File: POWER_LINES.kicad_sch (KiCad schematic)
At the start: 50 parts, among them J11 1717020, J12 1717020, J6 1730405, J8 1717020, J9 1717020, K3 G2R-1A-E DC5, K4 G2R-1A-E DC5, K5 G2R-1A-E DC5, K6 G2R-1A-E DC5, Q3 AO3400A, Q4 AO3400A

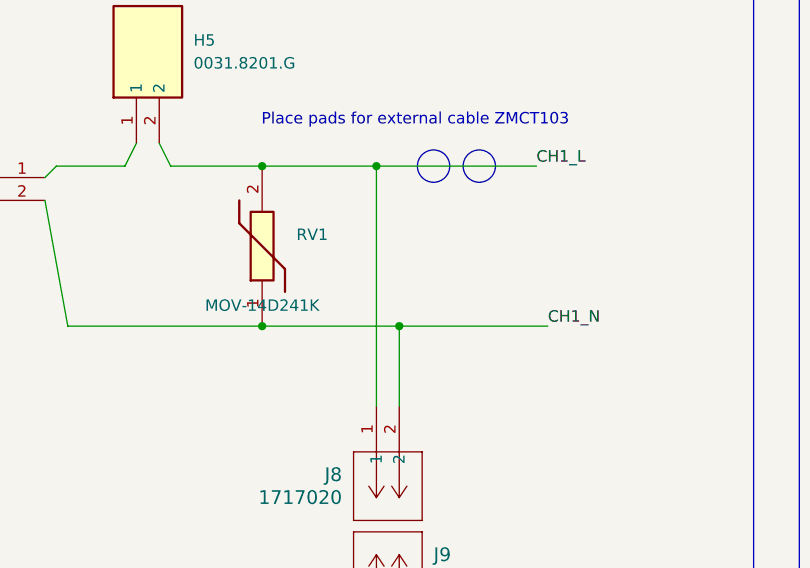
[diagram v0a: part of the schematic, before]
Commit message: add usb 2.0 speed selector
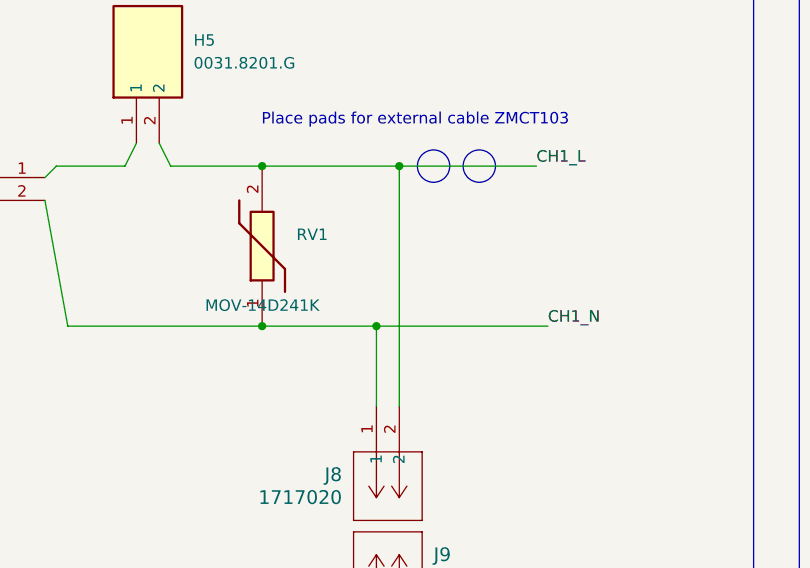
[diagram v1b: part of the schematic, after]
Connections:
- net CH1_L: now also J8.2; no longer J8.1
- net CH1_N: now also J8.1; no longer J8.2
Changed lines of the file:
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@@
 	)
 	(junction
-		(at 203.2 102.87)
+		(at 123.19 49.53)
 		(diameter 0)
 		(color 0 0 0 0)
 	)
 	(junction
-		(at 110.49 31.75)
+		(at 203.2 102.87)
 		(diameter 0)
 		(color 0 0 0 0)
 	)
 	(junction
-		(at 125.73 49.53)
+		(at 110.49 31.75)
 		(diameter 0)
 		(color 0 0 0 0)
@@
 	)
 	(junction
+		(at 125.73 31.75)
+		(diameter 0)
+		(color 0 0 0 0)
+	)
+	(junction
 		(at 66.04 137.16)
 		(diameter 0)
@@
 		(color 0 0 0 0)
 	)
-	(junction
-		(at 123.19 31.75)
-		(diameter 0)
-		(color 0 0 0 0)
-	)
 	(wire
 		(pts
@@
 	(wire
 		(pts
+			(xy 125.73 31.75) (xy 140.97 31.75)
+		)
+		(stroke
+			(width 0)
+			(type default)
+		)
+	)
+	(wire
+		(pts
 			(xy 25.4 158.75) (xy 33.02 158.75)
 		)
@@
 	(wire
 		(pts
-			(xy 110.49 31.75) (xy 140.97 31.75)
+			(xy 110.49 31.75) (xy 125.73 31.75)
 		)
 		(stroke
@@
 	(wire
 		(pts
-			(xy 125.73 49.53) (xy 125.73 58.42)
-		)
-		(stroke
-			(width 0)
-			(type default)
-		)
-	)
-	(wire
-		(pts
 			(xy 59.69 137.16) (xy 66.04 137.16)
 		)
@@
 	(wire
 		(pts
-			(xy 99.06 29.21) (xy 100.33 31.75)
+			(xy 123.19 49.53) (xy 123.19 58.42)
 		)
 		(stroke
@@
 	(wire
 		(pts
-			(xy 203.2 119.38) (xy 203.2 137.16)
+			(xy 99.06 29.21) (xy 100.33 31.75)
 		)
 		(stroke
@@
 	(wire
 		(pts
-			(xy 125.73 49.53) (xy 142.24 49.53)
+			(xy 203.2 119.38) (xy 203.2 137.16)
 		)
 		(stroke
@@
 	(wire
 		(pts
-			(xy 123.19 31.75) (xy 123.19 58.42)
+			(xy 204.47 45.72) (xy 204.47 62.23)
 		)
 		(stroke
@@
 	(wire
 		(pts
-			(xy 204.47 45.72) (xy 204.47 62.23)
+			(xy 204.47 29.21) (xy 204.47 38.1)
 		)
 		(stroke
@@
 	(wire
 		(pts
-			(xy 204.47 29.21) (xy 204.47 38.1)
+			(xy 218.44 53.34) (xy 218.44 59.69)
 		)
 		(stroke
@@
 	(wire
 		(pts
-			(xy 218.44 53.34) (xy 218.44 59.69)
+			(xy 266.7 135.89) (xy 271.78 135.89)
 		)
 		(stroke
@@
 	(wire
 		(pts
-			(xy 266.7 135.89) (xy 271.78 135.89)
+			(xy 113.03 168.91) (xy 116.84 168.91)
 		)
 		(stroke
@@
 	(wire
 		(pts
-			(xy 113.03 168.91) (xy 116.84 168.91)
+			(xy 66.04 173.99) (xy 66.04 176.53)
 		)
 		(stroke
@@
 	(wire
 		(pts
-			(xy 66.04 173.99) (xy 66.04 176.53)
+			(xy 132.08 125.73) (xy 132.08 123.19)
 		)
 		(stroke
@@
 	(wire
 		(pts
-			(xy 132.08 125.73) (xy 132.08 123.19)
+			(xy 125.73 31.75) (xy 125.73 58.42)
 		)
 		(stroke
@@
 	(wire
 		(pts
+			(xy 123.19 49.53) (xy 142.24 49.53)
+		)
+		(stroke
+			(width 0)
+			(type default)
+		)
+	)
+	(wire
+		(pts
 			(xy 95.25 31.75) (xy 96.52 29.21)
 		)
@@
 	(wire
 		(pts
-			(xy 110.49 49.53) (xy 125.73 49.53)
+			(xy 110.49 49.53) (xy 123.19 49.53)
 		)
 		(stroke
@@
 		(in_pos_files yes)
 		(dnp no)
-		(fields_autoplaced yes)
 		(property "Reference" "J9"
 			(at 129.54 74.9299 90)

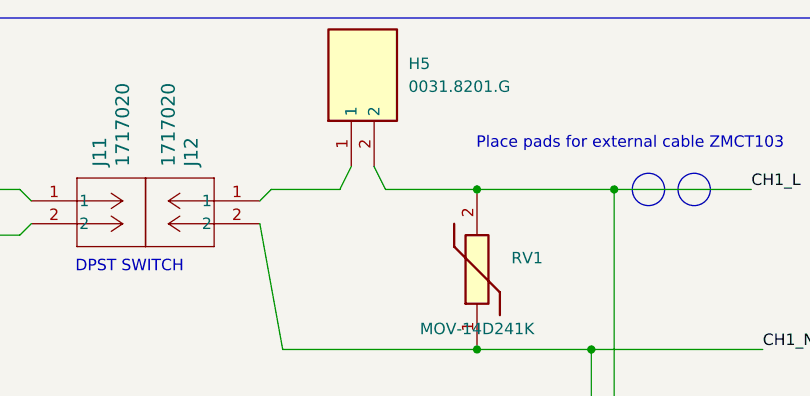
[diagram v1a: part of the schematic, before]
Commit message: add leds
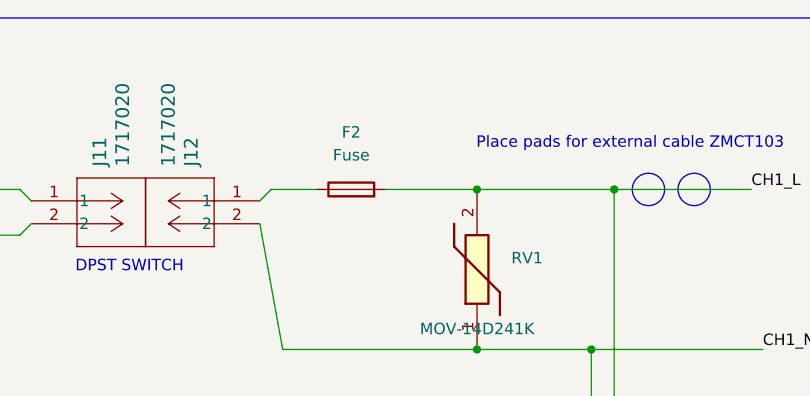
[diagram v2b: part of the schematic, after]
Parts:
- F2: renamed from H5; value 0031.8201.G -> Fuse; symbol SamacSys_Parts:0031.8201.G -> Device:Fuse
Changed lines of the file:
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@@
 	(wire
 		(pts
-			(xy 100.33 31.75) (xy 110.49 31.75)
-		)
-		(stroke
-			(width 0)
-			(type default)
-		)
-	)
-	(wire
-		(pts
 			(xy 60.96 107.95) (xy 60.96 104.14)
 		)
@@
 	(wire
 		(pts
-			(xy 87.63 31.75) (xy 95.25 31.75)
+			(xy 87.63 31.75) (xy 92.71 31.75)
 		)
 		(stroke
@@
 	(wire
 		(pts
-			(xy 99.06 29.21) (xy 100.33 31.75)
+			(xy 100.33 31.75) (xy 110.49 31.75)
 		)
 		(stroke
@@
 	(wire
 		(pts
-			(xy 95.25 31.75) (xy 96.52 29.21)
-		)
-		(stroke
-			(width 0)
-			(type default)
-		)
-	)
-	(wire
-		(pts
 			(xy 203.2 100.33) (xy 203.2 102.87)
 		)
@@
 	)
 	(symbol
-		(lib_id "SamacSys_Parts:0031.8201.G")
-		(at 96.52 29.21 90)
+		(lib_id "Device:Fuse")
+		(at 96.52 31.75 90)
 		(unit 1)
 		(body_style 1)
@@
 		(dnp no)
 		(fields_autoplaced yes)
-		(property "Reference" "H5"
-			(at 102.87 17.7799 90)
+		(property "Reference" "F2"
+			(at 96.52 25.4 90)
 			(show_name no)
 			(do_not_autoplace no)
@@
 					(size 1.27 1.27)
 				)
-				(justify right)
 			)
 		)
-		(property "Value" "0031.8201.G"
-			(at 102.87 20.3199 90)
+		(property "Value" "Fuse"
+			(at 96.52 27.94 90)
 			(show_name no)
 			(do_not_autoplace no)
@@
 					(size 1.27 1.27)
 				)
-				(justify right)
 			)
 		)
 		(property "Footprint" "SmartSupplyLib:fuse holder"
-			(at 191.44 12.7 0)
+			(at 96.52 33.528 90)
 			(hide yes)
 			(show_name no)
@@
 					(size 1.27 1.27)
 				)
-				(justify left top)
 			)
 		)
 		(property "Datasheet" "https://www.schurter.com/en/datasheet/ogn"
-			(at 291.44 12.7 0)
+			(at 96.52 31.75 0)
 			(hide yes)
 			(show_name no)
@@
 					(size 1.27 1.27)
 				)
-				(justify left top)
 			)
 		)
-		(property "Description" "OGN for THT 22.5mm"
-			(at 96.52 29.21 0)
+		(property "Description" "Fuse"
+			(at 96.52 31.75 0)
 			(hide yes)
 			(show_name no)
@@
 		)
 		(property "Height" "12.7"
-			(at 491.44 12.7 0)
+			(at 491.44 15.24 0)
 			(hide yes)
 			(show_name no)
@@
 		)
 		(property "Mouser Part Number" "693-0031.8201.G"
-			(at 591.44 12.7 0)
+			(at 591.44 15.24 0)
 			(hide yes)
 			(show_name no)
@@
 		)
 		(property "Mouser Price/Stock" "https://www.mouser.co.uk/ProductDetail/Schurter/0031.8201.G?qs=53fxdJjyGHQ26HnfkWkpvg%3D%3D"
-			(at 691.44 12.7 0)
+			(at 691.44 15.24 0)
 			(hide yes)
 			(show_name no)
@@
 		)
 		(property "Manufacturer_Name" "SCHURTER"
-			(at 791.44 12.7 0)
+			(at 791.44 15.24 0)
 			(hide yes)
 			(show_name no)
@@
 		)
 		(property "Manufacturer_Part_Number" "0031.8201.G"
-			(at 891.44 12.7 0)
+			(at 891.44 15.24 0)
 			(hide yes)
 			(show_name no)
@@
 			(project "smart_supply"
 				(path "/487ef637-7a03-4925-80c1-798e0c6f0bbd/34ab41b0-567d-4411-99e8-070d64ace837"
-					(reference "H5")
+					(reference "F2")
 					(unit 1)
 				)

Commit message: minimal change
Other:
- moved on the sheet: F2, RV1
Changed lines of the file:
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@@
 	)
 	(circle
-		(center 134.62 31.75)
+		(center 134.62 22.86)
 		(radius 1.7961)
 		(stroke
@@
 	)
 	(circle
-		(center 129.54 31.75)
+		(center 129.54 22.86)
 		(radius 1.7961)
 		(stroke
@@
 	(text "Place pads for external cable ZMCT103"
 		(exclude_from_sim no)
-		(at 127.508 26.67 0)
+		(at 127.508 17.78 0)
 		(effects
 			(font
@@
 	)
 	(junction
-		(at 110.49 31.75)
+		(at 110.49 22.86)
 		(diameter 0)
 		(color 0 0 0 0)
@@
 	)
 	(junction
-		(at 125.73 31.75)
+		(at 125.73 22.86)
 		(diameter 0)
 		(color 0 0 0 0)
@@
 	(wire
 		(pts
+			(xy 86.36 35.56) (xy 87.63 35.56)
+		)
+		(stroke
+			(width 0)
+			(type default)
+		)
+	)
+	(wire
+		(pts
 			(xy 193.04 83.82) (xy 193.04 85.09)
 		)
@@
 	(wire
 		(pts
+			(xy 110.49 22.86) (xy 110.49 26.67)
+		)
+		(stroke
+			(width 0)
+			(type default)
+		)
+	)
+	(wire
+		(pts
 			(xy 127 101.6) (xy 132.08 101.6)
 		)
@@
 	(wire
 		(pts
-			(xy 125.73 31.75) (xy 140.97 31.75)
+			(xy 125.73 22.86) (xy 140.97 22.86)
 		)
 		(stroke
@@
 	(wire
 		(pts
+			(xy 87.63 49.53) (xy 110.49 49.53)
+		)
+		(stroke
+			(width 0)
+			(type default)
+		)
+	)
+	(wire
+		(pts
 			(xy 132.08 152.4) (xy 135.89 152.4)
 		)
@@
 	(wire
 		(pts
-			(xy 110.49 31.75) (xy 125.73 31.75)
+			(xy 110.49 22.86) (xy 125.73 22.86)
 		)
 		(stroke
@@
 	(wire
 		(pts
-			(xy 88.9 49.53) (xy 110.49 49.53)
-		)
-		(stroke
-			(width 0)
-			(type default)
-		)
-	)
-	(wire
-		(pts
 			(xy 217.17 127) (xy 217.17 133.35)
 		)
@@
 	(wire
 		(pts
-			(xy 88.9 49.53) (xy 86.36 35.56)
-		)
-		(stroke
-			(width 0)
-			(type default)
-		)
-	)
-	(wire
-		(pts
-			(xy 87.63 31.75) (xy 92.71 31.75)
+			(xy 102.87 186.69) (xy 113.03 186.69)
 		)
 		(stroke
@@
 	(wire
 		(pts
-			(xy 102.87 186.69) (xy 113.03 186.69)
+			(xy 87.63 35.56) (xy 87.63 49.53)
 		)
 		(stroke
@@
 	(wire
 		(pts
+			(xy 87.63 22.86) (xy 92.71 22.86)
+		)
+		(stroke
+			(width 0)
+			(type default)
+		)
+	)
+	(wire
+		(pts
+			(xy 110.49 44.45) (xy 110.49 49.53)
+		)
+		(stroke
+			(width 0)
+			(type default)
+		)
+	)
+	(wire
+		(pts
 			(xy 125.73 85.09) (xy 149.86 85.09)
 		)
@@
 	(wire
 		(pts
-			(xy 100.33 31.75) (xy 110.49 31.75)
+			(xy 100.33 22.86) (xy 110.49 22.86)
 		)
 		(stroke
@@
 	(wire
 		(pts
+			(xy 87.63 33.02) (xy 86.36 33.02)
+		)
+		(stroke
+			(width 0)
+			(type default)
+		)
+	)
+	(wire
+		(pts
 			(xy 247.65 55.88) (xy 247.65 62.23)
 		)
@@
 	(wire
 		(pts
-			(xy 86.36 33.02) (xy 87.63 31.75)
+			(xy 87.63 33.02) (xy 87.63 22.86)
 		)
 		(stroke
@@
 	(wire
 		(pts
-			(xy 125.73 31.75) (xy 125.73 58.42)
+			(xy 125.73 22.86) (xy 125.73 58.42)
 		)
 		(stroke
@@
 	)
 	(label "CH1_L"
-		(at 140.97 31.75 0)
+		(at 140.97 22.86 0)
 		(effects
 			(font
@@
 	(symbol
 		(lib_id "SmartSupplyLib:MOV-14D241K")
-		(at 110.49 49.53 90)
+		(at 110.49 44.45 90)
 		(unit 1)
 		(body_style 1)
@@
 		(dnp no)
 		(property "Reference" "RV1"
-			(at 114.3 39.3699 90)
+			(at 114.3 34.2899 90)
 			(show_name no)
 			(do_not_autoplace no)
@@
 		)
 		(property "Value" "MOV-14D241K"
-			(at 104.14 47.244 90)
+			(at 104.14 42.164 90)
 			(show_name no)
 			(do_not_autoplace no)
@@
 		)
 		(property "Footprint" "SmartSupplyLib:MOV14D241K"
-			(at 206.68 35.56 0)
+			(at 206.68 30.48 0)
 			(hide yes)
 			(show_name no)
@@
 		)
 		(property "Datasheet" "https://datasheet.datasheetarchive.com/originals/distributors/Datasheets-DGA16/858708.pdf"
-			(at 306.68 35.56 0)
+			(at 306.68 30.48 0)
 			(hide yes)
 			(show_name no)
@@
 		)
 		(property "Description" "Bourns MOV-14D Series Metal Oxide Varistor 830pF 50A 395V"
-			(at 110.49 49.53 0)
+			(at 110.49 44.45 0)
 			(hide yes)
 			(show_name no)
@@
 		)
 		(property "Height" "20"
-			(at 506.68 35.56 0)
+			(at 506.68 30.48 0)
 			(hide yes)
 			(show_name no)
@@
 		)
 		(property "Mouser Part Number" "652-MOV-14D241K"
-			(at 606.68 35.56 0)
+			(at 606.68 30.48 0)
 			(hide yes)
 			(show_name no)
@@
 		)
 		(property "Mouser Price/Stock" "https://www.mouser.co.uk/ProductDetail/Bourns/MOV-14D241K?qs=CQ3B1E%252BbPs2CiKalQN9uMQ%3D%3D"
-			(at 706.68 35.56 0)
+			(at 706.68 30.48 0)
 			(hide yes)
 			(show_name no)
@@
 		)
 		(property "Manufacturer_Name" "Bourns"
-			(at 806.68 35.56 0)
+			(at 806.68 30.48 0)
 			(hide yes)
 			(show_name no)
@@
 		)
 		(property "Manufacturer_Part_Number" "MOV-14D241K"
-			(at 906.68 35.56 0)
+			(at 906.68 30.48 0)
 			(hide yes)
 			(show_name no)
@@
 	(symbol
 		(lib_id "Device:Fuse")
-		(at 96.52 31.75 90)
+		(at 96.52 22.86 90)
 		(unit 1)
 		(body_style 1)
@@
 		(fields_autoplaced yes)
 		(property "Reference" "F2"
-			(at 96.52 25.4 90)
+			(at 96.52 16.51 90)
 			(show_name no)
 			(do_not_autoplace no)
@@
 		)
 		(property "Value" "Fuse"
-			(at 96.52 27.94 90)
+			(at 96.52 19.05 90)
 			(show_name no)
 			(do_not_autoplace no)
@@
 		)
 		(property "Footprint" "SmartSupplyLib:fuse holder"
-			(at 96.52 33.528 90)
+			(at 96.52 24.638 90)
 			(hide yes)
 			(show_name no)
@@
 		)
 		(property "Datasheet" "https://www.schurter.com/en/datasheet/ogn"
-			(at 96.52 31.75 0)
+			(at 96.52 22.86 0)
 			(hide yes)
 			(show_name no)
@@
 		)
 		(property "Description" "Fuse"
-			(at 96.52 31.75 0)
+			(at 96.52 22.86 0)
 			(hide yes)
 			(show_name no)
@@
 		)
 		(property "Height" "12.7"
-			(at 491.44 15.24 0)
+			(at 491.44 6.35 0)
 			(hide yes)
 			(show_name no)
@@
 		)
 		(property "Mouser Part Number" "693-0031.8201.G"
-			(at 591.44 15.24 0)
+			(at 591.44 6.35 0)
 			(hide yes)
 			(show_name no)
@@
 		)
 		(property "Mouser Price/Stock" "https://www.mouser.co.uk/ProductDetail/Schurter/0031.8201.G?qs=53fxdJjyGHQ26HnfkWkpvg%3D%3D"
-			(at 691.44 15.24 0)
+			(at 691.44 6.35 0)
 			(hide yes)
 			(show_name no)
@@
 		)
 		(property "Manufacturer_Name" "SCHURTER"
-			(at 791.44 15.24 0)
+			(at 791.44 6.35 0)
 			(hide yes)
 			(show_name no)
@@
 		)
 		(property "Manufacturer_Part_Number" "0031.8201.G"
-			(at 891.44 15.24 0)
+			(at 891.44 6.35 0)
 			(hide yes)
 			(show_name no)

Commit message: MPN BOOT BUTTON MINOR CHANGES
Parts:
- C39, C40, C41, C42, C43, C44, C45, C46: MPN (none) -> CC0805KRX7R9BB333
- Csns1, Csns2: MPN (none) -> ZMCT103C
- D10, D7, D8, D9: MPN (none) -> 1N4007
- F2: MPN (none) -> 0031.8201.G
- J11, J12, J8, J9: MPN (none) -> 1717020
- J6: MPN (none) -> 1730405
- K3, K4, K5, K6: MPN (none) -> G2R-1A-E-DC5
- Q3, Q4: MPN (none) -> AO3400A
- R26, R27: value 49.9k -> 47k; MPN (none) -> MFR01SF4702A10
- R28, R38, R50, R52: MPN (none) -> 0805W8F1000T5E
- R29, R30, R31, R34, R37, R39, R42, R43: MPN (none) -> 0805W8F1001T5E
- R32, R33: footprint Resistor_SMD:R_0805_2012Metric -> Resistor_SMD:R_0603_1608Metric; MPN (none) -> 0603WAF100JT5E
- R36: MPN (none) -> MFR0W4F2002A50
- R40, R41: footprint Resistor_SMD:R_0805_2012Metric -> Resistor_SMD:R_0603_1608Metric; MPN (none) -> 0603WAF330JT5E
- R51, R53: MPN (none) -> 0805W8F1003T5E
- RV1: MPN (none) -> MOV-14D241K
- Vsns1, Vsns2: MPN (none) -> ZMPT101K
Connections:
- net GND: now also R38.2; no longer R38.1
- net VP2: now also R39.2; no longer R39.1
- new net: R38.1, R39.1, Vsns2.4
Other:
- moved on the sheet: R38, R39

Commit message: FINAL SCHEMATIC
Global nets, more ESD safety, complete bom, outlets, other fixes, ERC CLEAN
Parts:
- added J14: 1730405, SmartSupplyLib:CONN_1730405_PXC, symbol SmartSupplyLib:1730405
- added J15: 1717020, SmartSupplyLib:CONN_1717020_PXC, symbol SmartSupplyLib:1717020
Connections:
- net CH1_L_OUT: now also J14.1
- net CH1_N_OUT: now also J14.3
- net CH2_L_OUT: now also J15.1
- net CH2_N_OUT: now also J15.2
- net PE: now also J14.2
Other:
- note added: "CH1 OUT"
- note added: "CH2 OUT"
- note added: "INLET FUSE SWITCH"
- note added: "OUTLETS"
- note added: "Relay CH2 L"
- note added: "Relay CH2 N"
- note removed: "Connector and fuse"
- moved on the sheet: D9, K3, R50, R52
